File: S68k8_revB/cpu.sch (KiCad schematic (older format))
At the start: 7 parts, among them U20 ATF16V8C, U21 MC68008FN

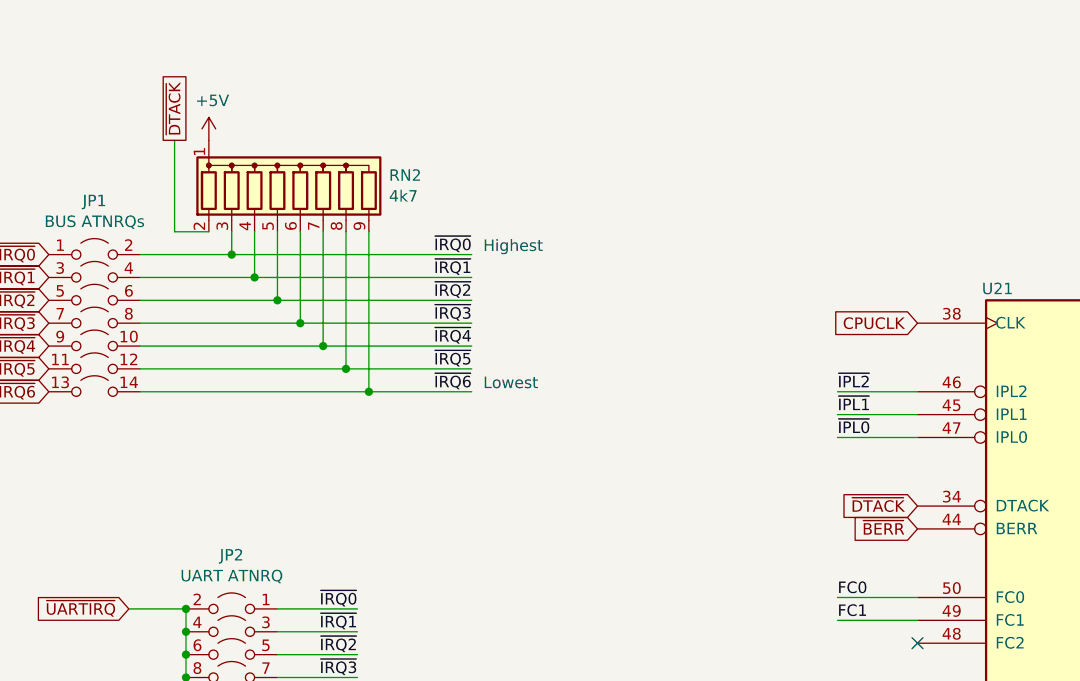
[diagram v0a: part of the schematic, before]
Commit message: S68k8: change pull-up for DTACK to a separate resistor
Tests show 4k7 is too large to pull the line back fast enough. Reducing to 1k or even 470R give much better results.
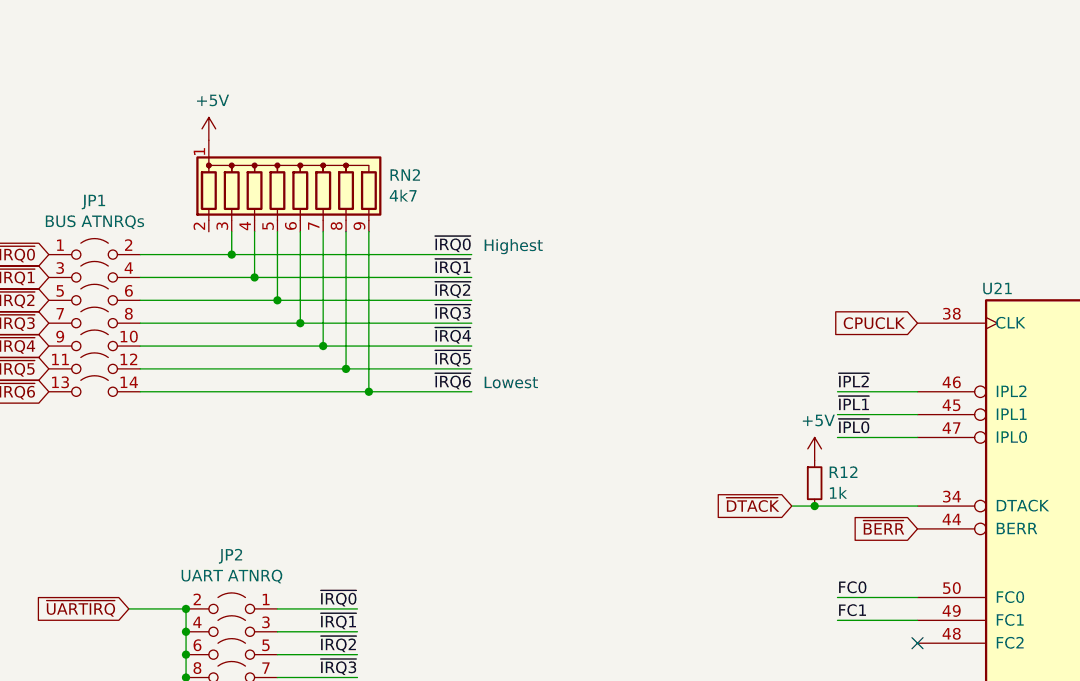
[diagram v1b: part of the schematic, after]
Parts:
- added R12: 1k, Resistor_THT:R_Axial_DIN0204_L3.6mm_D1.6mm_P7.62mm_Horizontal, symbol Device:R_Small
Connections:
- net +5V: now also R12.1
- net ~DTACK: now also R12.2; no longer RN2.2 (R1)
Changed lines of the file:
@@
 Text GLabel 6400 1800 0    50   Input ~ 0
 CPUCLK
-Text GLabel 6400 2600 0    50   Input ~ 0
+Text GLabel 5850 2600 0    50   Input ~ 0
 ~DTACK
 Text GLabel 6400 2700 0    50   Input ~ 0
@@
 Wire Wire Line
 	3000 2100 4000 2100
-Wire Wire Line
-	3300 1400 3150 1400
-Wire Wire Line
-	3150 1400 3150 1000
-Text GLabel 3150 1000 1    50   UnSpc ~ 0
-~DTACK
 NoConn ~ 2950 5750
 NoConn ~ 4050 5350
 NoConn ~ 4050 5450
 NoConn ~ 4050 5550
+Wire Wire Line
+	5850 2600 5950 2600
+$Comp
+L Device:R_Small R12
+U 1 1 600D3DDF
+P 5950 2500
+F 0 "R12" H 6009 2546 50  0000 L CNN
+F 1 "1k" H 6009 2455 50  0000 L CNN
+F 2 "Resistor_THT:R_Axial_DIN0204_L3.6mm_D1.6mm_P7.62mm_Horizontal" H 5950 2500 50  0001 C CNN
+F 3 "~" H 5950 2500 50  0001 C CNN
+	1    5950 2500
+	1    0    0    -1
+$EndComp
+Connection ~ 5950 2600
+Wire Wire Line
+	5950 2600 6400 2600
+$Comp
+L power:+5V #PWR076
+U 1 1 600D43CE
+P 5950 2400
+F 0 "#PWR076" H 5950 2250 50  0001 C CNN
+F 1 "+5V" H 5965 2573 50  0000 C CNN
+F 2 "" H 5950 2400 50  0001 C CNN
+F 3 "" H 5950 2400 50  0001 C CNN
+	1    5950 2400
+	1    0    0    -1
+$EndComp
 $EndSCHEMATC
